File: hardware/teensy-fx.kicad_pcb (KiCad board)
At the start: 4 copper layers, 60 x 100 mm, 84 parts, among them J1 AudioJack3_Ground, J2 AudioJack3_Ground, J3 AudioJack3_Ground, SW1 Switch_SW_Push, SW2 Switch_SW_Push, SW3 Switch_SW_Push, SW4 Switch_SW_Push, U1 Teensy4.0, U2 AP7313-1.8V, U3 SGTL5000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

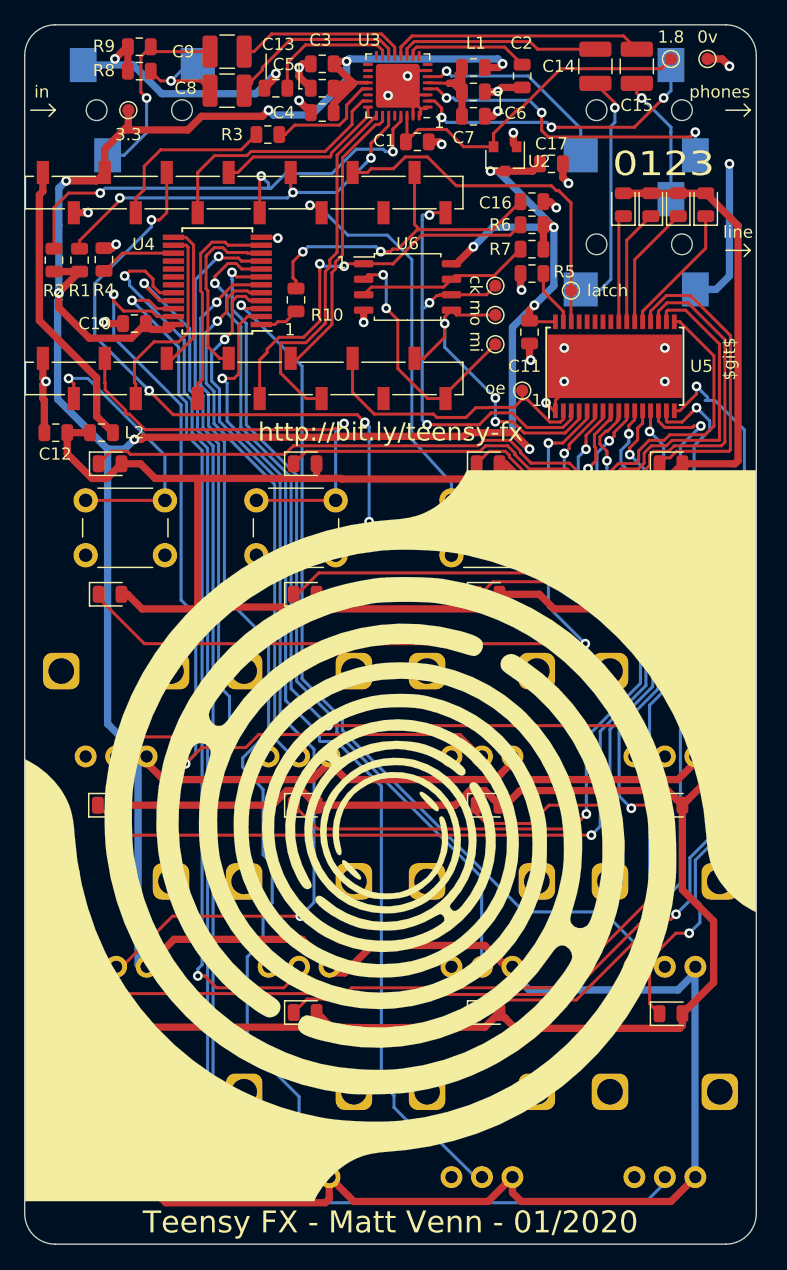
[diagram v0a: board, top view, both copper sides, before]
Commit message: changed to LDO that I can source from farnell
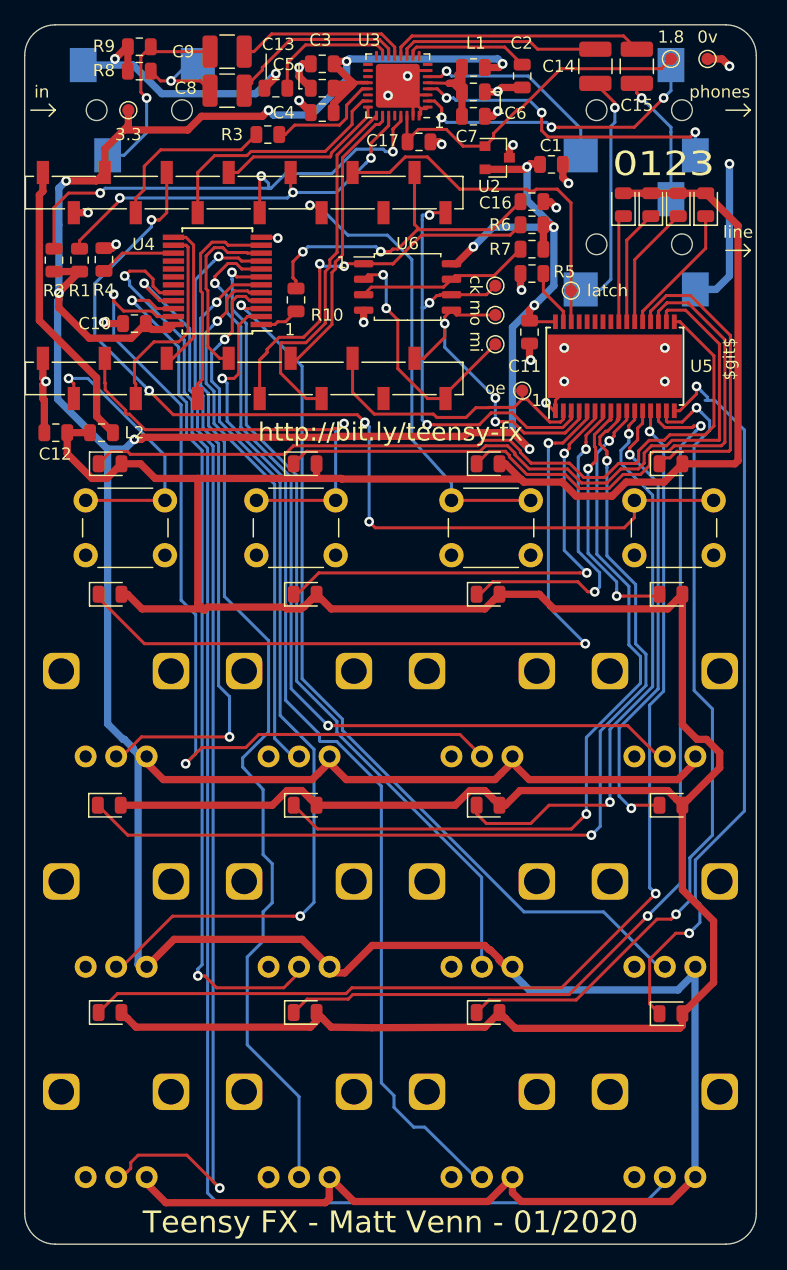
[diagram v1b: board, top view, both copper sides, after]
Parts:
- removed G*** (x2): LOGO, audio-fx:back-graphic
- U2: value AP7313-1.8V -> MCP1811A
- moved C1 11.2 mm to (268.2, 56.5)
- moved C17 11.0 mm to (257.3, 54.6)
- moved U2 0.66 mm to (263.8, 55.9), turned to 0 degrees
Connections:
- C1 pad 1: +1V8 -> +3V3
- C17 pad 1: +3V3 -> +1V8
- U2 pad 1: GND -> +1V8
- U2 pad 2: +1V8 -> +3V3
- U2 pad 3: +3V3 -> GND
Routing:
- net +3V3: track 397.1 -> 396.2 mm
- net +1V8: track 28.6 -> 27.9 mm

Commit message: date format change
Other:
- board text added: "Teensy FX - Matt Venn - 2020/01"
- board text removed: "Teensy FX - Matt Venn - 01/2020"
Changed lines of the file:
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@@
   (gr_line (start 264 50.5) (end 264 52.25) (layer F.SilkS) (width 0.12))
   (gr_line (start 263.25 50.5) (end 264 50.5) (layer F.SilkS) (width 0.12))
-  (gr_text "Teensy FX - Matt Venn - 01/2020" (at 255 143.2) (layer F.SilkS)
+  (gr_text "Teensy FX - Matt Venn - 2020/01" (at 255 143.2) (layer F.SilkS)
     (effects (font (size 1.8 1.8) (thickness 0.35)))
   )

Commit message: fix library mess and get bom exported
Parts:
- R10: value 200r -> 100R
- R5: value 5k -> 4.7k
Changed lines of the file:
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@@
       (effects (font (size 1 1) (thickness 0.15)))
     )
-    (fp_text value 5k (at 0 1.65) (layer F.Fab)
+    (fp_text value 4.7k (at 0 1.65) (layer F.Fab)
       (effects (font (size 1 1) (thickness 0.15)))
     )
@@
       (effects (font (size 1 1) (thickness 0.15)))
     )
-    (fp_text value 200r (at 0 1.65 90) (layer F.Fab)
-      (effects (font (size 1 1) (thickness 0.15)))
-    )
+    (fp_text value 100R (at 0 1.65 90) (layer F.Fab)
+      (effects (font (size 1 1) (thickness 0.15)))
+    )

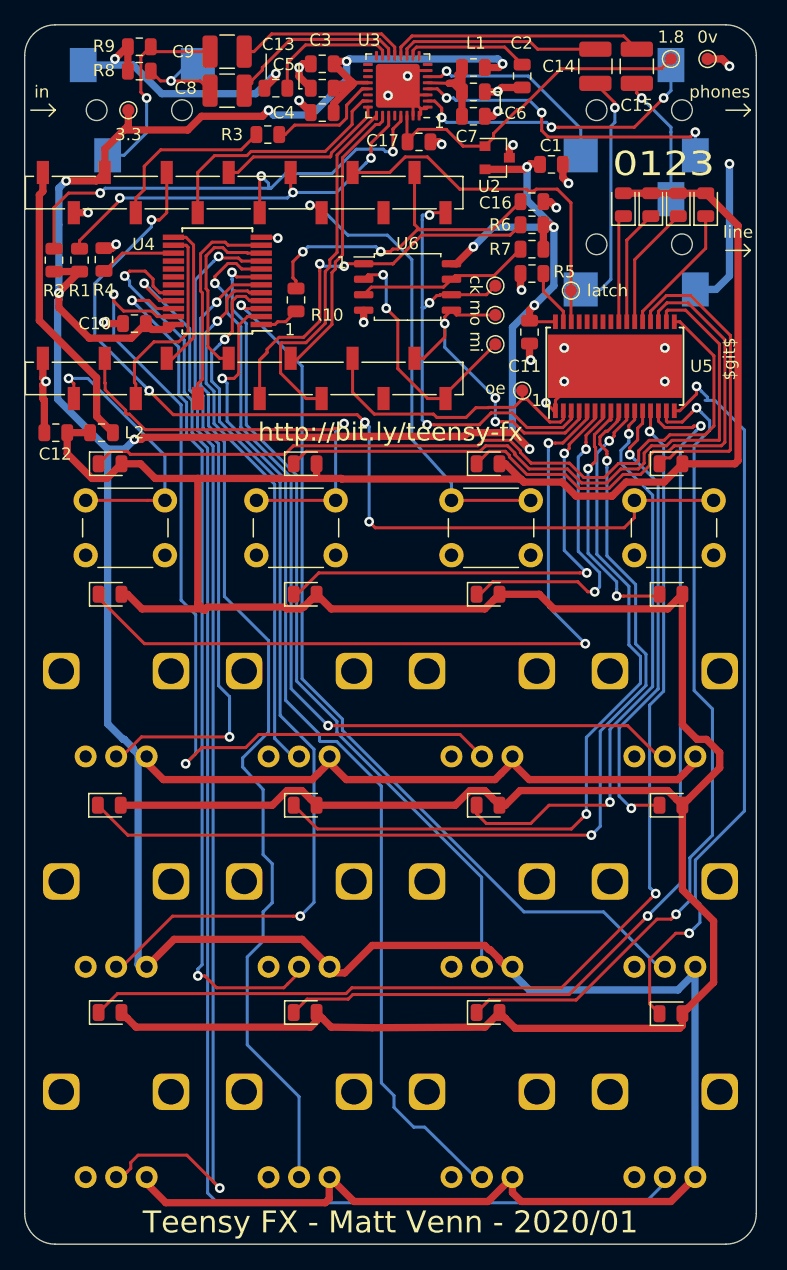
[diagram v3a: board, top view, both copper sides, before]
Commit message: missing silk graphics!
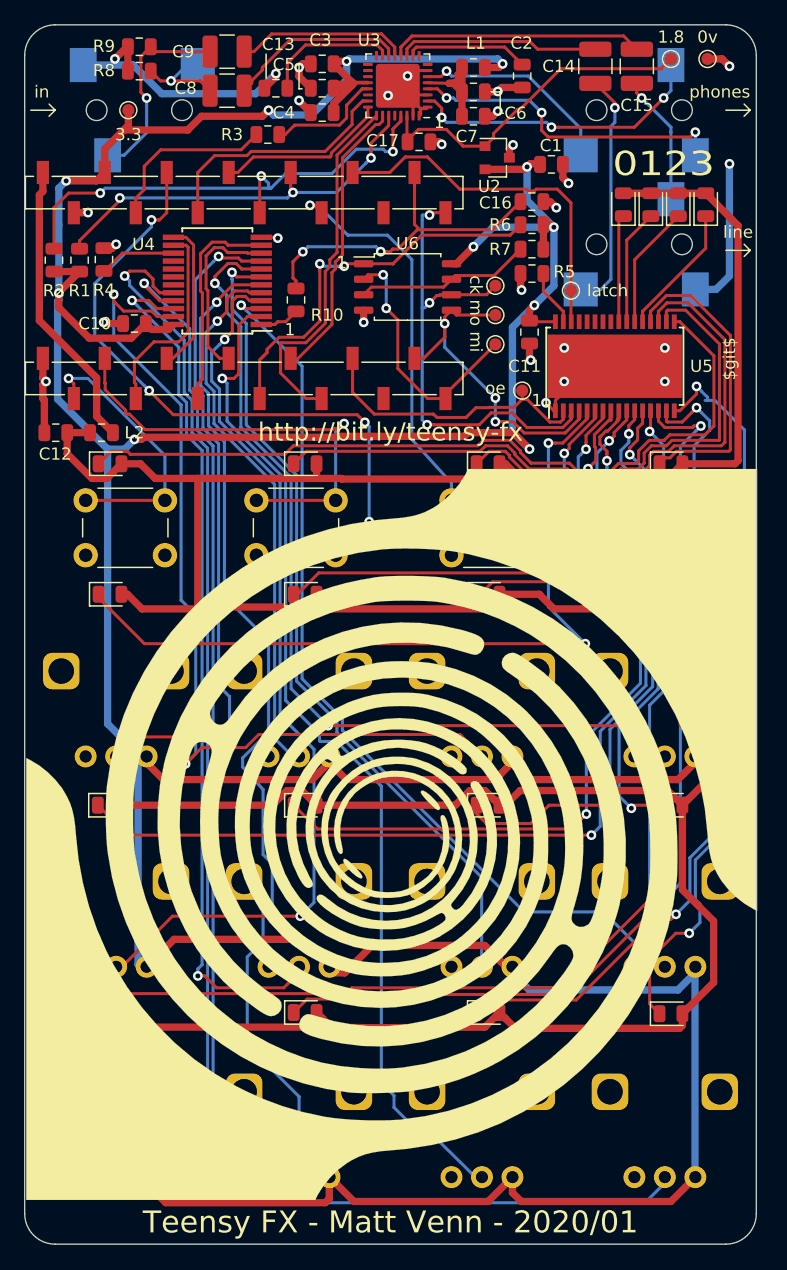
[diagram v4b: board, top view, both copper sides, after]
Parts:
- added G***: LOGO, audio-fx:back-graphic, B.Cu at (255.0, 111.3)
- added G***: LOGO, audio-fx:back-graphic, F.Cu at (255.1, 111.4)

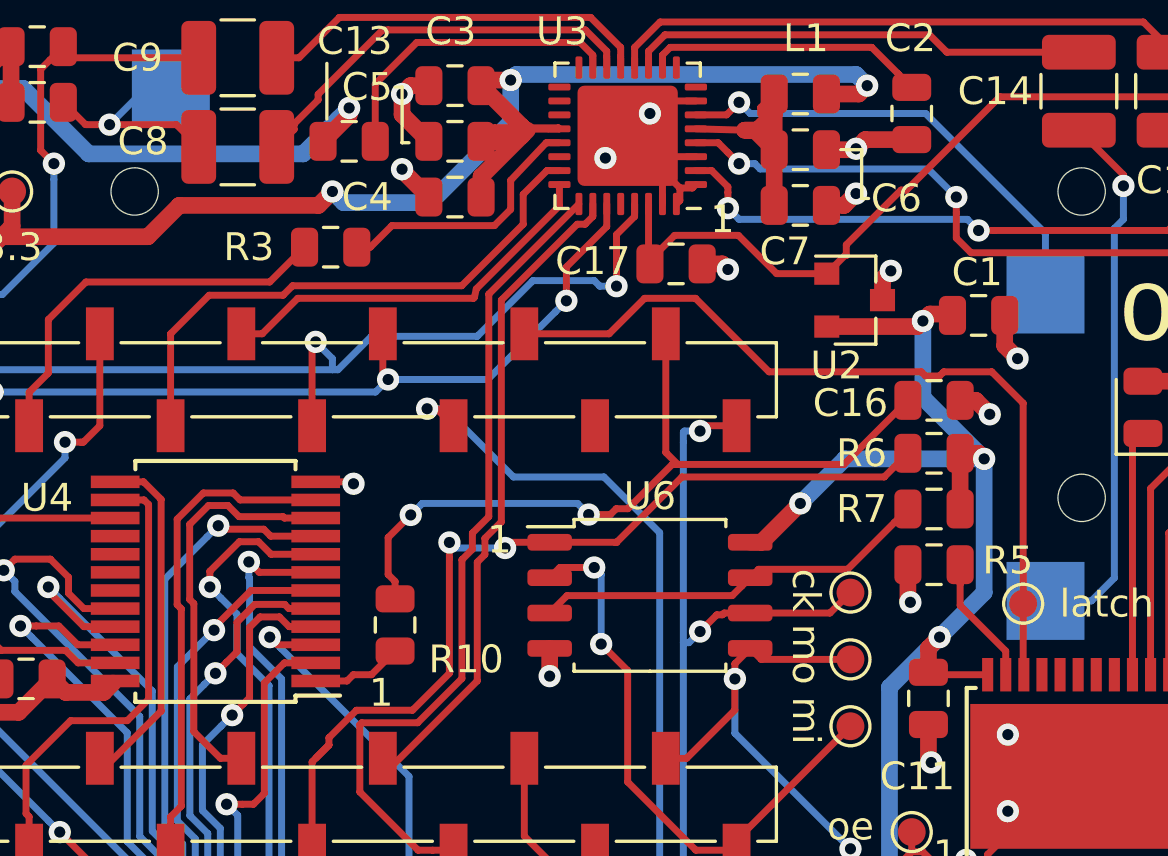
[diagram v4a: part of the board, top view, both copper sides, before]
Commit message: fix wiring & routing for lrclk and bclk, and removed lp filter behind pot mux
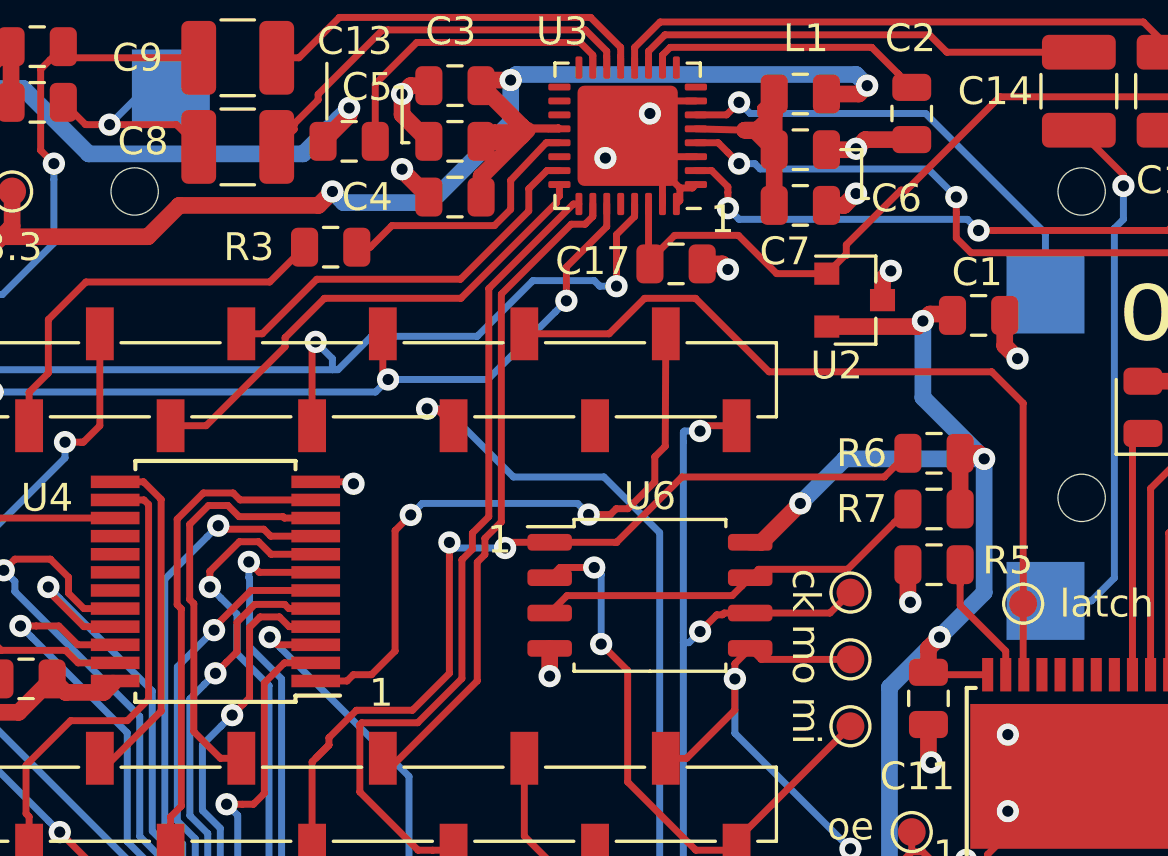
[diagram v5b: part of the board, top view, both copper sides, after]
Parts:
- removed C16: 2.2uF, Capacitor_SMD:C_0805_2012Metric
- removed R10: 100R, Resistor_SMD:R_0805_2012Metric
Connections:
- U3 pad 23: BCLK -> LRCLK
- U3 pad 24: LRCLK -> BCLK
- U4 pad 1: Net-(R10-Pad1) -> pot_multiplex
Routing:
- net pot_multiplex: track 28.2 -> 23.6 mm
- net Net-(R10-Pad1): track 3.47 -> 0.00 mm
- net BCLK: track 20.3 -> 18.1 mm
- net GND: track 87.7 -> 86.4 mm, vias 27 -> 26
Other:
- board text added: "2 approved DRC errors"
